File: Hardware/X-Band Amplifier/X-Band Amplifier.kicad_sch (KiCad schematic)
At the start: 11 parts, among them J1 901-10513-3, J2 901-10513-3, U1 QPA1022

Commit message: Updating Board
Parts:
- removed H7, H8: 4-40, _tim-Mounting-Holes:2-56_Hole_Pad, symbol Mechanical:MountingHole_Pad
- added TP1: TestPoint, TestPoint:TestPoint_Pad_D1.0mm, symbol Connector:TestPoint
- H5, H6: value 4-40 -> 2-56
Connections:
- net at U1.16 (VDET): now also TP1.1
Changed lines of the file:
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@@
 	(wire
 		(pts
-			(xy 107.95 130.81) (xy 107.95 132.08)
+			(xy 88.9 130.81) (xy 88.9 132.08)
 		)
 		(stroke
@@
 	(wire
 		(pts
-			(xy 88.9 130.81) (xy 88.9 132.08)
+			(xy 82.55 130.81) (xy 82.55 132.08)
 		)
 		(stroke
@@
 	(wire
 		(pts
-			(xy 82.55 130.81) (xy 82.55 132.08)
+			(xy 105.41 63.5) (xy 107.95 63.5)
 		)
 		(stroke
@@
 	(wire
 		(pts
-			(xy 105.41 63.5) (xy 107.95 63.5)
+			(xy 95.25 130.81) (xy 95.25 132.08)
 		)
 		(stroke
@@
 	(wire
 		(pts
-			(xy 101.6 130.81) (xy 101.6 132.08)
+			(xy 128.27 46.99) (xy 128.27 48.26)
 		)
 		(stroke
@@
 	(wire
 		(pts
-			(xy 95.25 130.81) (xy 95.25 132.08)
+			(xy 138.43 63.5) (xy 140.97 63.5)
 		)
 		(stroke
@@
 	(wire
 		(pts
-			(xy 138.43 63.5) (xy 140.97 63.5)
+			(xy 63.5 130.81) (xy 63.5 132.08)
 		)
 		(stroke
@@
 	(wire
 		(pts
-			(xy 63.5 130.81) (xy 63.5 132.08)
+			(xy 123.19 78.74) (xy 123.19 80.01)
 		)
 		(stroke
@@
 	(wire
 		(pts
-			(xy 123.19 78.74) (xy 123.19 80.01)
+			(xy 76.2 130.81) (xy 76.2 132.08)
 		)
 		(stroke
@@
 	(wire
 		(pts
-			(xy 76.2 130.81) (xy 76.2 132.08)
+			(xy 100.33 68.58) (xy 100.33 69.85)
 		)
 		(stroke
@@
 	(wire
 		(pts
-			(xy 100.33 68.58) (xy 100.33 69.85)
+			(xy 146.05 68.58) (xy 146.05 69.85)
 		)
 		(stroke
@@
 	(wire
 		(pts
-			(xy 146.05 68.58) (xy 146.05 69.85)
+			(xy 69.85 130.81) (xy 69.85 132.08)
 		)
 		(stroke
@@
 		)
 	)
-	(wire
-		(pts
-			(xy 69.85 130.81) (xy 69.85 132.08)
-		)
-		(stroke
-			(width 0)
-			(type default)
-		)
-	)
 	(symbol
 		(lib_id "Mechanical:MountingHole_Pad")
@@
 			)
 		)
-		(property "Value" "4-40"
+		(property "Value" "2-56"
 			(at 92.456 124.46 0)
 			(effects
@@
 	)
 	(symbol
-		(lib_id "power:GND")
-		(at 107.95 132.08 0)
-		(unit 1)
-		(exclude_from_sim no)
-		(in_bom yes)
-		(on_board yes)
-		(dnp no)
-		(property "Reference" "#PWR011"
-			(at 107.95 138.43 0)
-			(effects
-				(font
-					(size 1.27 1.27)
-				)
-				(hide yes)
-			)
-		)
-		(property "Value" "GND"
-			(at 107.95 135.89 0)
-			(effects
-				(font
-					(size 1.27 1.27)
-				)
-			)
-		)
-		(property "Footprint" ""
-			(at 107.95 132.08 0)
-			(effects
-				(font
-					(size 1.27 1.27)
-				)
-				(hide yes)
-			)
-		)
-		(property "Datasheet" ""
-			(at 107.95 132.08 0)
-			(effects
-				(font
-					(size 1.27 1.27)
-				)
-				(hide yes)
-			)
-		)
-		(property "Description" "Power symbol creates a global label with name \"GND\" , ground"
-			(at 107.95 132.08 0)
-			(effects
-				(font
-					(size 1.27 1.27)
-				)
-				(hide yes)
-			)
-		)
-		(pin "1"
-		)
-		(instances
-			(project "X-Band Amplifier"
-				(path "/267aea38-9020-4ce0-aad2-ef3514cc22e2"
-					(reference "#PWR011")
-					(unit 1)
-				)
-			)
-		)
-	)
-	(symbol
 		(lib_id "_tim-RF:QPA1022")
 		(at 123.19 63.5 0)
@@
 				(path "/267aea38-9020-4ce0-aad2-ef3514cc22e2"
 					(reference "#PWR09")
-					(unit 1)
-				)
-			)
-		)
-	)
-	(symbol
-		(lib_id "Mechanical:MountingHole_Pad")
-		(at 101.6 128.27 0)
-		(unit 1)
-		(exclude_from_sim no)
-		(in_bom yes)
-		(on_board yes)
-		(dnp no)
-		(property "Reference" "H7"
-			(at 100.33 122.682 0)
-			(effects
-				(font
-					(size 1.27 1.27)
-				)
-				(justify left)
-			)
-		)
-		(property "Value" "4-40"
-			(at 98.806 124.46 0)
-			(effects
-				(font
-					(size 1.27 1.27)
-				)
-				(justify left)
-			)
-		)
-		(property "Footprint" "_tim-Mounting-Holes:2-56_Hole_Pad"
-			(at 101.6 128.27 0)
-			(effects
-				(font
-					(size 1.27 1.27)
-				)
-				(hide yes)
-			)
-		)
-		(property "Datasheet" "~"
-			(at 101.6 128.27 0)
-			(effects
-				(font
-					(size 1.27 1.27)
-				)
-				(hide yes)
-			)
-		)
-		(property "Description" "Mounting Hole with connection"
-			(at 101.6 128.27 0)
-			(effects
-				(font
-					(size 1.27 1.27)
-				)
-				(hide yes)
-			)
-		)
-		(pin "1"
-		)
-		(instances
-			(project "X-Band Amplifier"
-				(path "/267aea38-9020-4ce0-aad2-ef3514cc22e2"
-					(reference "H7")
 					(unit 1)
 				)
@@
 	)
 	(symbol
-		(lib_id "power:GND")
-		(at 101.6 132.08 0)
-		(unit 1)
-		(exclude_from_sim no)
-		(in_bom yes)
-		(on_board yes)
-		(dnp no)
-		(property "Reference" "#PWR010"
-			(at 101.6 138.43 0)
-			(effects
-				(font
-					(size 1.27 1.27)
-				)
-				(hide yes)
-			)
-		)
-		(property "Value" "GND"
-			(at 101.6 135.89 0)
-			(effects
-				(font
-					(size 1.27 1.27)
-				)
-			)
-		)
-		(property "Footprint" ""
-			(at 101.6 132.08 0)
-			(effects
-				(font
-					(size 1.27 1.27)
-				)
-				(hide yes)
-			)
-		)
-		(property "Datasheet" ""
-			(at 101.6 132.08 0)
-			(effects
-				(font
-					(size 1.27 1.27)
-				)
-				(hide yes)
-			)
-		)
-		(property "Description" "Power symbol creates a global label with name \"GND\" , ground"
-			(at 101.6 132.08 0)
-			(effects
-				(font
-					(size 1.27 1.27)
-				)
-				(hide yes)
-			)
-		)
-		(pin "1"
-		)
-		(instances
-			(project "X-Band Amplifier"
-				(path "/267aea38-9020-4ce0-aad2-ef3514cc22e2"
-					(reference "#PWR010")
+		(lib_id "Connector:TestPoint")
+		(at 128.27 46.99 0)
+		(unit 1)
+		(exclude_from_sim no)
+		(in_bom no)
+		(on_board yes)
+		(dnp no)
+		(property "Reference" "TP1"
+			(at 131.572 44.704 0)
+			(effects
+				(font
+					(size 1.27 1.27)
+				)
+				(justify left)
+			)
+		)
+		(property "Value" "TestPoint"
+			(at 129.032 46.736 0)
+			(effects
+				(font
+					(size 1.27 1.27)
+				)
+				(justify left)
+			)
+		)
+		(property "Footprint" "TestPoint:TestPoint_Pad_D1.0mm"
+			(at 133.35 46.99 0)
+			(effects
+				(font
+					(size 1.27 1.27)
+				)
+				(hide yes)
+			)
+		)
+		(property "Datasheet" "~"
+			(at 133.35 46.99 0)
+			(effects
+				(font
+					(size 1.27 1.27)
+				)
+				(hide yes)
+			)
+		)
+		(property "Description" "test point"
+			(at 128.27 46.99 0)
+			(effects
+				(font
+					(size 1.27 1.27)
+				)
+				(hide yes)
+			)
+		)
+		(pin "1"
+		)
+		(instances
+			(project "X-Band Amplifier"
+				(path "/267aea38-9020-4ce0-aad2-ef3514cc22e2"
+					(reference "TP1")
 					(unit 1)
 				)
@@
 				(path "/267aea38-9020-4ce0-aad2-ef3514cc22e2"
 					(reference "H1")
-					(unit 1)
-				)
-			)
-		)
-	)
-	(symbol
-		(lib_id "Mechanical:MountingHole_Pad")
-		(at 107.95 128.27 0)
-		(unit 1)
-		(exclude_from_sim no)
-		(in_bom yes)
-		(on_board yes)
-		(dnp no)
-		(property "Reference" "H8"
-			(at 106.68 122.682 0)
-			(effects
-				(font
-					(size 1.27 1.27)
-				)
-				(justify left)
-			)
-		)
-		(property "Value" "4-40"
-			(at 105.156 124.46 0)
-			(effects
-				(font
-					(size 1.27 1.27)
-				)
-				(justify left)
-			)
-		)
-		(property "Footprint" "_tim-Mounting-Holes:2-56_Hole_Pad"
-			(at 107.95 128.27 0)
-			(effects
-				(font
-					(size 1.27 1.27)
-				)
-				(hide yes)
-			)
-		)
-		(property "Datasheet" "~"
-			(at 107.95 128.27 0)
-			(effects
-				(font
-					(size 1.27 1.27)
-				)
-				(hide yes)
-			)
-		)
-		(property "Description" "Mounting Hole with connection"
-			(at 107.95 128.27 0)
-			(effects
-				(font
-					(size 1.27 1.27)
-				)
-				(hide yes)
-			)
-		)
-		(pin "1"
-		)
-		(instances
-			(project "X-Band Amplifier"
-				(path "/267aea38-9020-4ce0-aad2-ef3514cc22e2"
-					(reference "H8")
 					(unit 1)
 				)
@@
 			)
 		)
-		(property "Value" "4-40"
+		(property "Value" "2-56"
 			(at 86.106 124.46 0)
 			(effects

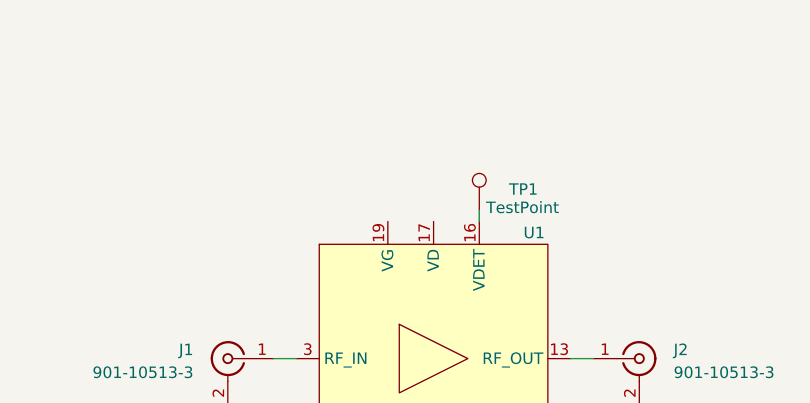
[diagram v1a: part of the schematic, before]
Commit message: Adding capacitors
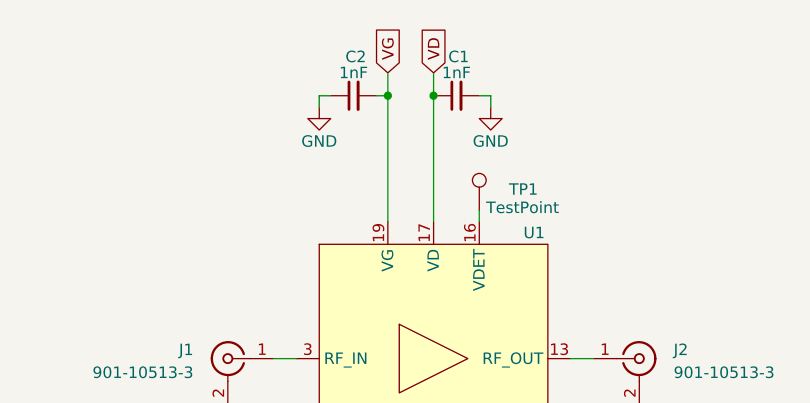
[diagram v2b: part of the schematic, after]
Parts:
- added C1, C2: 1nF, Capacitor_SMD:C_0402_1005Metric, symbol Device:C_Small
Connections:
- net GND: now also C1.2, C2.1
- net VD: now reaches U1.17 (VD)
- net VD: now also C1.1
- net VG: now reaches U1.19 (VG)
- net VG: now also C2.2
